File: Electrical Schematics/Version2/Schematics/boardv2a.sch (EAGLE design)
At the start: 622 parts, among them IC1 MCP41HVX1ST, IC2 ADUM4160BRW, IC3 SE555D, IC5 74LVC1G04DBV, IC6 74LVC1G04DBV, IC7 4030D, K1 G5V-2, K2 CP1SA-12V, Q1 IRLML2060TRPBFBSS123LT1G, Q10 IRLML2060TRPBFBSS123LT1G, Q11 IRLML2060TRPBFBSS123LT1G, Q12 IRLML2060TRPBFBSS123LT1G, Q13 IRLML2060TRPBFBSS123LT1G, Q17 IRLML2060TRPBFBSS123LT1G, Q18 MOSFET-PCHANNEL, Q19 IRLML2060TRPBFBSS123LT1G, Q2 IRLML2060TRPBFBSS123LT1G, Q3 IRLML2060TRPBFBSS123LT1G, Q4 MOSFET-PCHANNEL, Q5 MOSFET-PCHANNEL, Q6 IRLML2060TRPBFBSS123LT1G, Q7 ASFL1, Q8 IRLML2060TRPBFBSS123LT1G, Q9 IRLML2060TRPBFBSS123LT1G, U1 CP2130-GM, U10 SN65HVDA100-Q1_D_8, U11 ADUM3442CRWZ, U12 ADUM3442CRWZ, U13 ADUM3442CRWZ, U14 ADUM3442CRWZ, U15 ADUM3442CRWZ, U16 ADUM3442CRWZ, U17 ADUM3442CRWZ, U18 LM1085_KTT_3, U19 ADUM3442CRWZ, U2 TMS570LS0432_PZ_100, U20 ADUM3442CRWZ, U3 LM1085_KTT_3, U4 LM1085_KTT_3, U5 LM1084_KTT_3, U6 TPS3514_D_14, U7 LM1085_KTT_3, U9 ADUM3442CRWZ, X4 5566-4

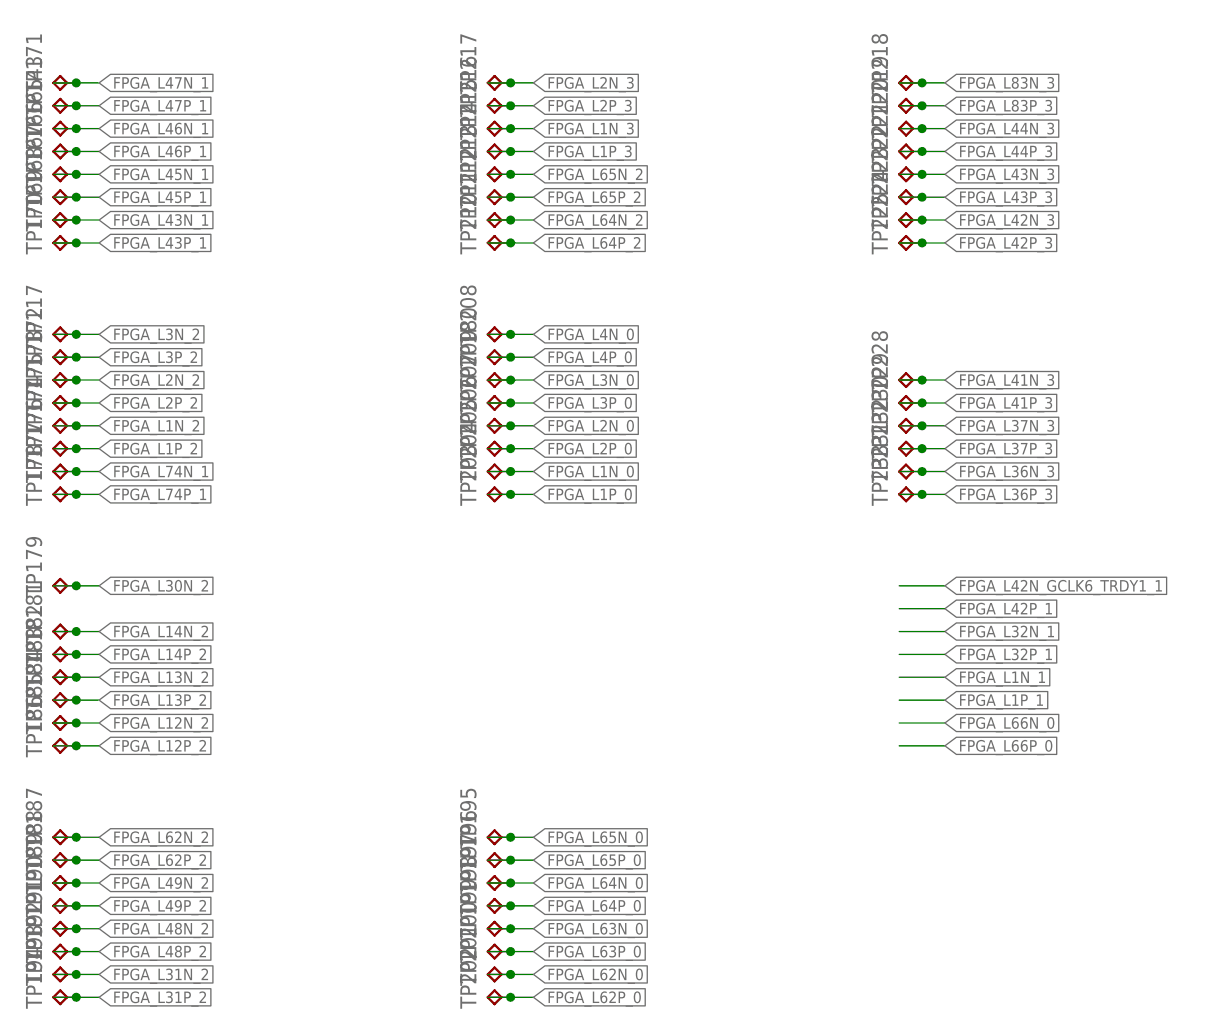
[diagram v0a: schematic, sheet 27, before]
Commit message: fpga to mcu
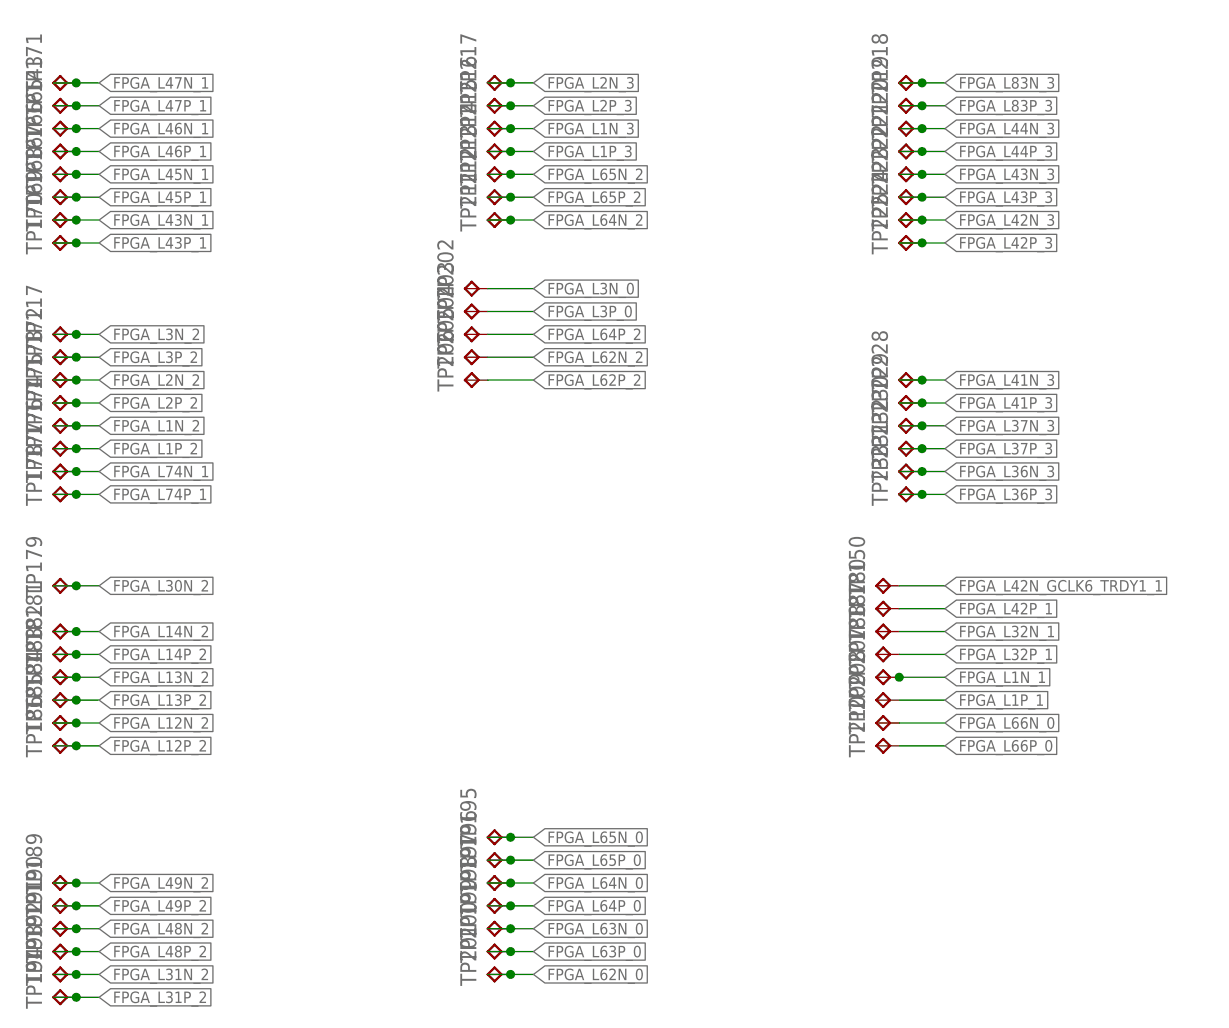
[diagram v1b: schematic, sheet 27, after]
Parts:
- added TP150: TPPAD1-13, testpad:TPPAD1-13
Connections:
- net FPGA_MCU_AD1_RES renamed N$307
- net FPGA_MCU_AD2_RES renamed N$308
- net FPGA_MCU_AD3_RES renamed N$309
- net FPGA_MCU_AD4_RES renamed N$310
- net FPGA_MCU_AD5_RES renamed N$311
- net FPGA_MCU_AD6_RES renamed N$312
- net FPGA_MCU_ADO_RES renamed N$306
- removed net FPGA_L1N_0: TP204.TP, U$6.IO_L1N_VREF_0
- removed net FPGA_L1P_0: TP203.TP, U$6.IO_L1P_HSWAPEN_0
- removed net FPGA_L2N_0: TP206.TP, U$6.IO_L2N_0
- removed net FPGA_L2P_0: TP205.TP, U$6.IO_L2P_0
- removed net FPGA_L4N_0: TP208.TP
- removed net FPGA_L4P_0: TP180.TP
- removed net FPGA_L62P_0: TP202.TP
- removed net FPGA_MCU_RES: U$6.IO_L3N_0
- new net N$313: TP140.TP, U2.ADIN[6]
- net FPGA_L1N_1: now also TP207.TP
- net FPGA_L1P_1: now also TP208.TP
- net FPGA_L32N_1: now also TP187.TP
- net FPGA_L32P_1: now also TP188.TP
- net FPGA_L3N_0: now also TP202.TP, U$6.IO_L3N_0; no longer TP209.TP
- net FPGA_L3P_0: now also TP203.TP, U$6.IO_L3P_0; no longer TP207.TP
- net FPGA_L42N_GCLK6_TRDY1_1: now also TP150.TP
- net FPGA_L42P_1: now also TP180.TP
- net FPGA_L62N_2: now also TP205.TP, U$6.IO_L62N_D6_2; no longer TP187.TP
- net FPGA_L62P_2: now also TP206.TP, U$6.IO_L62P_D5_2; no longer TP188.TP
- net FPGA_L64P_2: now also TP204.TP, U$6.IO_L64P_D8_2; no longer TP210.TP
- net FPGA_L66N_0: now also TP209.TP
- net FPGA_L66P_0: now also TP210.TP
- net FPGA_MCU_AD7_RES: no longer TP140.TP, U2.ADIN[6]
- net FPGA_MCU_RES1: now also U$6.IO_L1P_HSWAPEN_0; no longer U$6.IO_L3P_0
- net FPGA_MCU_RES2: now also U$6.IO_L1N_VREF_0; no longer U$6.IO_L64P_D8_2
- net FPGA_MCU_RES3: now also U$6.IO_L2P_0; no longer U$6.IO_L62N_D6_2
- net FPGA_MCU_RES4: now also U$6.IO_L2N_0; no longer U$6.IO_L62P_D5_2
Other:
- moved on the sheet: TP180, TP187, TP188, TP202, TP203, TP204, TP205, TP206, TP207, TP208, TP209, TP210

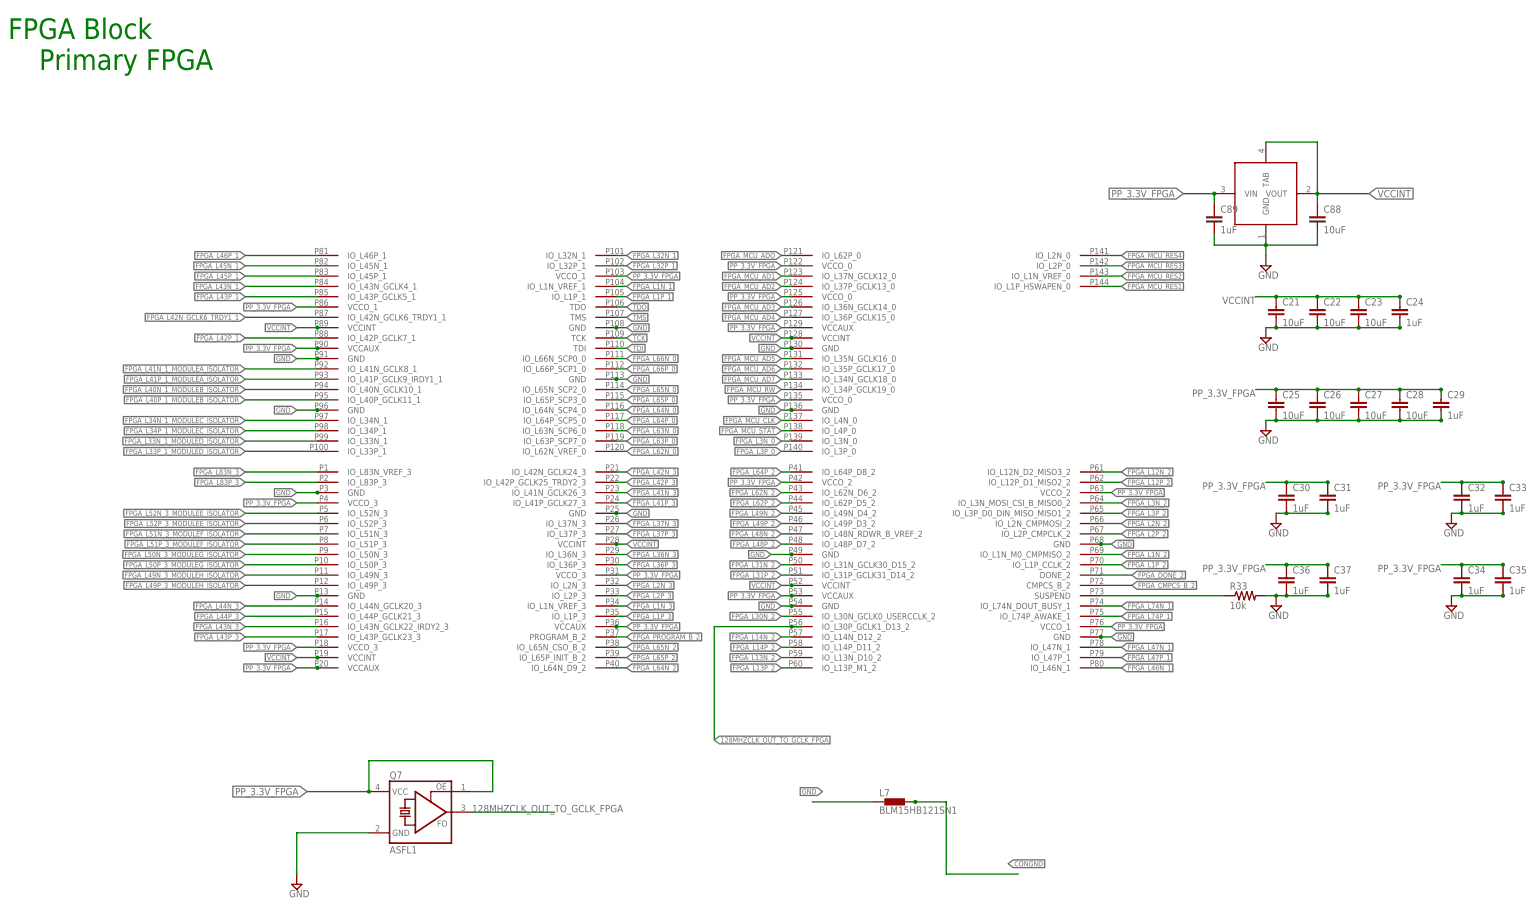
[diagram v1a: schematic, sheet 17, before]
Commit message: Fixed FPGA isolation routing
TODO: Check the FPGA pin by pin in the datasheet.
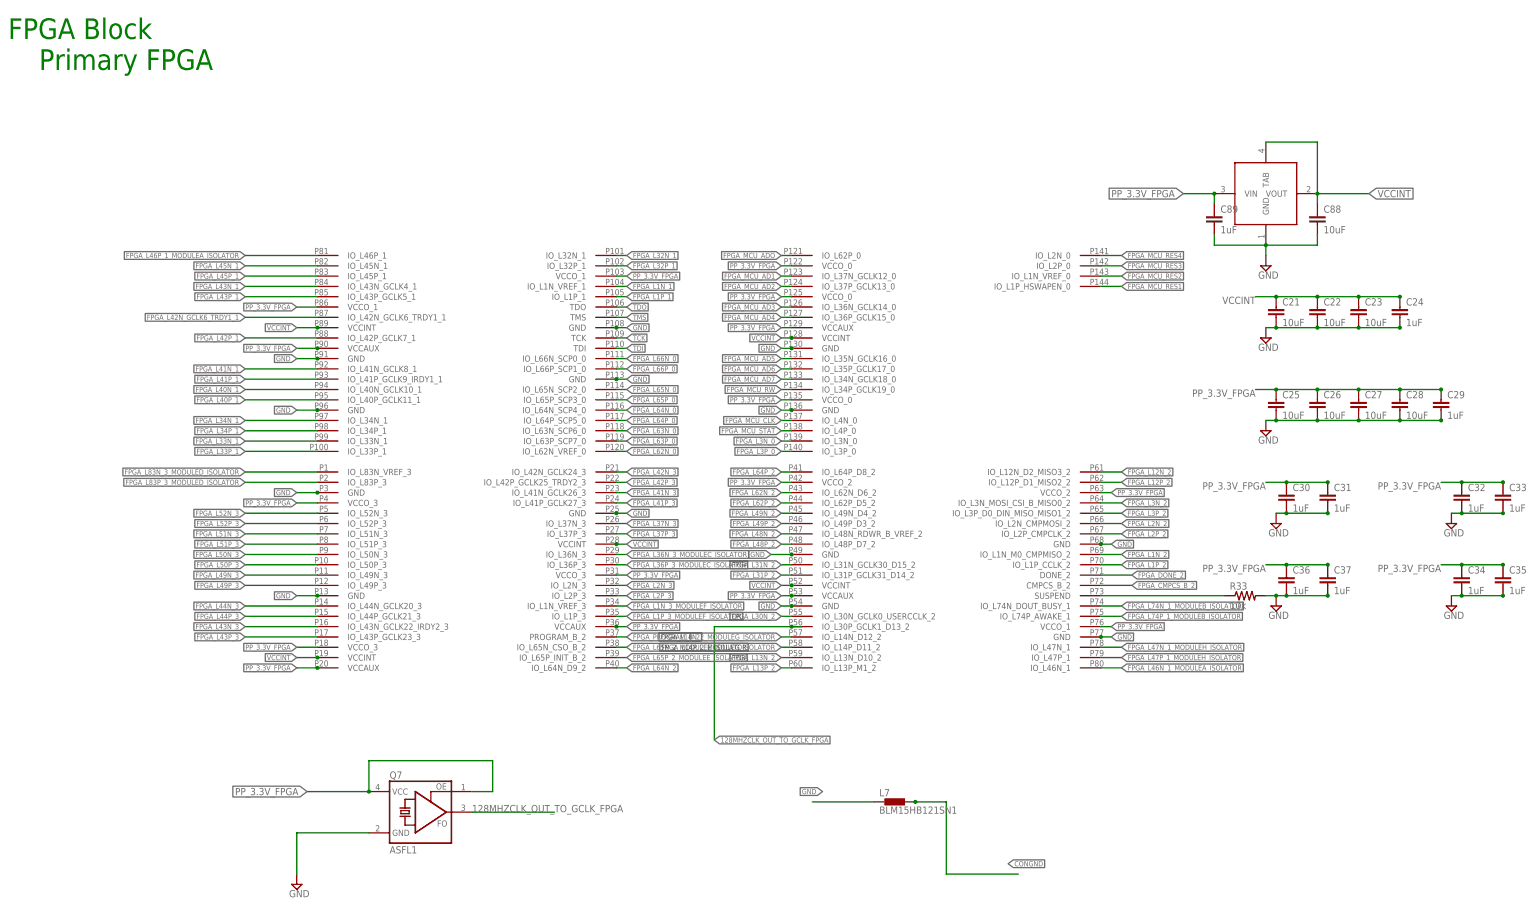
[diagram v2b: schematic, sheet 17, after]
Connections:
- removed net FPGA_L14N_2: TP181.TP, U$6.IO_L14N_D12_2
- removed net FPGA_L14P_2: TP182.TP, U$6.IO_L14P_D11_2
- removed net FPGA_L1N_3: TP215.TP, U$6.IO_L1N_VREF_3
- removed net FPGA_L1P_3: TP214.TP, U$6.IO_L1P_3
- removed net FPGA_L33N_1_MODULED_ISOLATOR: U$20.COM2, U$6.IO_L33N_1
- removed net FPGA_L33P_1_MODULED_ISOLATOR: U$23.COM2, U$6.IO_L33P_1
- removed net FPGA_L34N_1_MODULEC_ISOLATOR: U$18.COM2, U$6.IO_L34N_1
- removed net FPGA_L34P_1_MODULEC_ISOLATOR: U$19.COM2, U$6.IO_L34P_1
- removed net FPGA_L36N_3: TP231.TP, U$6.IO_L36N_3
- removed net FPGA_L36P_3: TP233.TP, U$6.IO_L36P_3
- removed net FPGA_L40N_1_MODULEB_ISOLATOR: U$16.COM2, U$6.IO_L40N_GCLK10_1
- removed net FPGA_L40P_1_MODULEB_ISOLATOR: U$17.COM2, U$6.IO_L40P_GCLK11_1
- removed net FPGA_L41N_1_MODULEA_ISOLATOR: U$13.COM2, U$6.IO_L41N_GCLK8_1
- removed net FPGA_L41P_1_MODULEA_ISOLATOR: U$14.COM2, U$6.IO_L41P_GCLK9_IRDY1_1
- removed net FPGA_L46N_1: TP165.TP, U$6.IO_L46N_1
- removed net FPGA_L46P_1: TP166.TP, U$6.IO_L46P_1
- removed net FPGA_L47N_1: TP171.TP, U$6.IO_L47N_1
- removed net FPGA_L47P_1: TP143.TP, U$6.IO_L47P_1
- removed net FPGA_L49N_3_MODULEH_ISOLATOR: U$30.COM2, U$6.IO_L49N_3
- removed net FPGA_L49P_3_MODULEH_ISOLATOR: U$31.COM2, U$6.IO_L49P_3
- removed net FPGA_L50N_3_MODULEG_ISOLATOR: U$28.COM2, U$6.IO_L50N_3
- removed net FPGA_L50P_3_MODULEG_ISOLATOR: U$29.COM2, U$6.IO_L50P_3
- removed net FPGA_L51N_3_MODULEF_ISOLATOR: U$26.COM2, U$6.IO_L51N_3
- removed net FPGA_L51P_3_MODULEF_ISOLATOR: U$27.COM2, U$6.IO_L51P_3
- removed net FPGA_L52N_3_MODULEE_ISOLATOR: U$24.COM2, U$6.IO_L52N_3
- removed net FPGA_L52P_3_MODULEE_ISOLATOR: U$25.COM2, U$6.IO_L52P_3
- removed net FPGA_L65N_2: TP213.TP, U$6.IO_L65N_CSO_B_2
- removed net FPGA_L65P_2: TP212.TP, U$6.IO_L65P_INIT_B_2
- removed net FPGA_L74N_1: TP177.TP, U$6.IO_L74N_DOUT_BUSY_1
- removed net FPGA_L74P_1: TP178.TP, U$6.IO_L74P_AWAKE_1
- removed net FPGA_L83N_3: TP218.TP, U$6.IO_L83N_VREF_3
- removed net FPGA_L83P_3: TP219.TP, U$6.IO_L83P_3
- new net FPGA_L14N_2_MODULEG_ISOLATOR: U$28.COM2, U$6.IO_L14N_D12_2
- new net FPGA_L14P_2_MODULEG_ISOLATOR: U$29.COM2, U$6.IO_L14P_D11_2
- new net FPGA_L1N_3_MODULEF_ISOLATOR: U$27.COM2, U$6.IO_L1N_VREF_3
- new net FPGA_L1P_3_MODULEF_ISOLATOR: U$26.COM2, U$6.IO_L1P_3
- new net FPGA_L33N_1: TP218.TP, U$6.IO_L33N_1
- new net FPGA_L33P_1: TP219.TP, U$6.IO_L33P_1
- new net FPGA_L34N_1: TP231.TP, U$6.IO_L34N_1
- new net FPGA_L34P_1: TP233.TP, U$6.IO_L34P_1
- new net FPGA_L36N_3_MODULEC_ISOLATOR: U$19.COM2, U$6.IO_L36N_3
- new net FPGA_L36P_3_MODULEC_ISOLATOR: U$18.COM2, U$6.IO_L36P_3
- new net FPGA_L40N_1: TP177.TP, U$6.IO_L40N_GCLK10_1
- new net FPGA_L40P_1: TP178.TP, U$6.IO_L40P_GCLK11_1
- new net FPGA_L41N_1: TP165.TP, U$6.IO_L41N_GCLK8_1
- new net FPGA_L41P_1: TP166.TP, U$6.IO_L41P_GCLK9_IRDY1_1
- new net FPGA_L46N_1_MODULEA_ISOLATOR: U$13.COM2, U$6.IO_L46N_1
- new net FPGA_L46P_1_MODULEA_ISOLATOR: U$14.COM2, U$6.IO_L46P_1
- new net FPGA_L47N_1_MODULEH_ISOLATOR: U$30.COM2, U$6.IO_L47N_1
- new net FPGA_L47P_1_MODULEH_ISOLATOR: U$31.COM2, U$6.IO_L47P_1
- new net FPGA_L49N_3: TP171.TP, U$6.IO_L49N_3
- new net FPGA_L49P_3: TP143.TP, U$6.IO_L49P_3
- new net FPGA_L50N_3: TP181.TP, U$6.IO_L50N_3
- new net FPGA_L50P_3: TP182.TP, U$6.IO_L50P_3
- new net FPGA_L51N_3: TP215.TP, U$6.IO_L51N_3
- new net FPGA_L51P_3: TP214.TP, U$6.IO_L51P_3
- new net FPGA_L52N_3: TP213.TP, U$6.IO_L52N_3
- new net FPGA_L52P_3: TP212.TP, U$6.IO_L52P_3
- new net FPGA_L65N_2_MODULEE_ISOLATOR: U$24.COM2, U$6.IO_L65N_CSO_B_2
- new net FPGA_L65P_2_MODULEE_ISOLATOR: U$25.COM2, U$6.IO_L65P_INIT_B_2
- new net FPGA_L74N_1_MODULEB_ISOLATOR: U$16.COM2, U$6.IO_L74N_DOUT_BUSY_1
- new net FPGA_L74P_1_MODULEB_ISOLATOR: U$17.COM2, U$6.IO_L74P_AWAKE_1
- new net FPGA_L83N_3_MODULED_ISOLATOR: U$23.COM2, U$6.IO_L83N_VREF_3
- new net FPGA_L83P_3_MODULED_ISOLATOR: U$20.COM2, U$6.IO_L83P_3

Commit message: routed more traces
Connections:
- net 5V_SU_J renamed 5V_SU_J123
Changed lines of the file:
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@@
 </segment>
 </net>
-<net name="5V_SU_J" class="0">
+<net name="5V_SU_J123" class="0">
 <segment>
 <wire x1="26.67" y1="90.17" x2="27.94" y2="90.17" width="0.1524" layer="91"/>

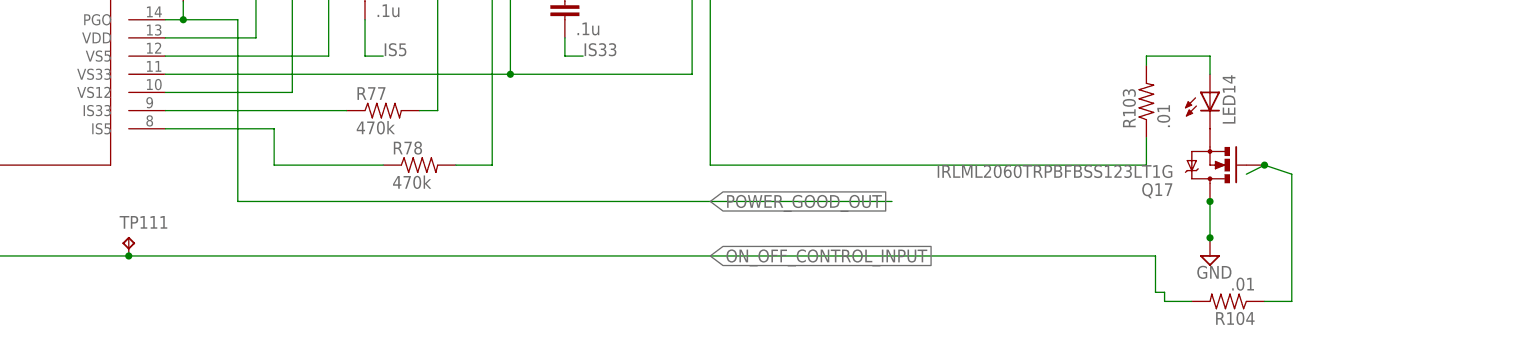
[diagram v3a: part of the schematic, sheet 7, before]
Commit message: Cap Placement and routing
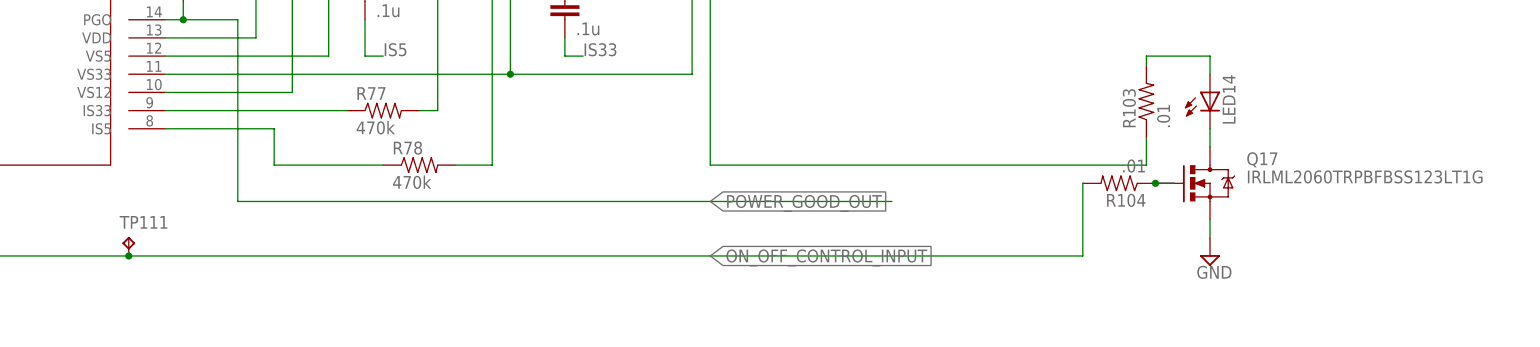
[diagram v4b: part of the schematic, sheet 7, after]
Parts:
- added C17: 10uF, SparkFun-Capacitors:CAP0603-CAP
- added C18: 1uF, SparkFun-Capacitors:CAP0603-CAP
- added R34, R41, R42: 10k, SparkFun-Passives:RESISTOR0603-RES
- added U$33: 1.2VREG, shit:1.2VREG
- TP216, TP217: value TPPAD1-13 -> TPB1,27; device testpad:TPPAD1-13 -> testpad:TPB1,27
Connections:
- removed net FPGA_L2N_3: TP217.TP, U$6.IO_L2N_3
- removed net FPGA_L2P_3: TP216.TP, U$6.IO_L2P_3
- removed net FPGA_L65N_2_MODULEE_ISOLATOR: U$24.COM2, U$6.IO_L65N_CSO_B_2
- removed net FPGA_L65P_2_MODULEE_ISOLATOR: U$25.COM2, U$6.IO_L65P_INIT_B_2
- removed net N$115: LED14.C, Q17.S
- new net FPGA_L2N_3_MODULEE_ISOLATOR: U$24.COM2, U$6.IO_L1N_VREF_3
- new net FPGA_L2P_3_MODULEE_ISOLATOR: U$25.COM2, U$6.IO_L1P_3
- new net FPGA_L65N_2: U$6.IO_L65N_CSO_B_2
- new net FPGA_PROGRAM_B: R42.1, U$6.IO_L65P_INIT_B_2
- new net N$12: LED14.C, Q17.D
- net CON_MONB_-: now also U19.GND2, U20.GND2
- net FPGA_DONE_2: now also R34.1
- net FPGA_L1N_3_MODULEF_ISOLATOR: now also U$6.IO_L2N_3; no longer U$6.IO_L1N_VREF_3
- net FPGA_L1P_3_MODULEF_ISOLATOR: now also U$6.IO_L2P_3; no longer U$6.IO_L1P_3
- net FPGA_PROGRAM_B_2: now also R41.1
- net GND: now also C17.2, C18.2, Q12.S, Q17.S, U$33.GND; no longer Q12.D, Q17.D
- net MCU_+1.2V: now also C17.1, U$33.TAB, U$33.VOUT
- net MCU_+3.3V: now also C18.1, U$33.VIN
- net N$185: now also TP216.TP
- net N$193: now also TP217.TP
- net N$26: now also R2401.2
- net N$63: now also Q12.D; no longer Q12.S
- net PP_3.3V_FPGA: now also R34.2, R41.2, R42.2
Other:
- moved on the sheet: Q12, Q17, R104, R2401, R29

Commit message: connector and routing
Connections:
- removed net CON_RELAY_HIGHSIDE: X4-4.S
- removed net FNR_CON_GROUND: U$5.P$6
- net 12V_SUPERVISED: now also U$5.P$6; no longer U$5.P$19
- net 5V_SUPERVISED: now also X4-4.S
- net CON_FIN: now also U$5.P$16; no longer U$5.P$14
- net CON_FNR_HIGH: now also U$5.P$11; no longer U$5.P$18
- net CON_FNR_POTGND: now also U$5.P$12; no longer U$5.P$16
- net CON_MONB_+: now also U$5.P$4; no longer U$5.P$9
- net CON_MONB_-: now also U$5.P$5; no longer U$5.P$10
- net CON_MONC_+: now also U$5.P$9; no longer U$5.P$11
- net CON_MONC_-: now also U$5.P$20; no longer U$5.P$12
- net CON_MONC_SP: now also U$5.P$10; no longer U$5.P$17
- net CON_NIN: now also U$5.P$17; no longer U$5.P$15
- net FNR_CON_F: now also U$5.P$15; no longer U$5.P$1
- net FNR_CON_R: now also U$5.P$14; no longer U$5.P$2
- net FNR_CON_THROTTLE-: now also U$5.P$2; no longer U$5.P$4
- net FNR_CON_THROTTLEWIPER: now also U$5.P$1; no longer U$5.P$5
- net GND: now also U$5.P$18, U$5.P$19; no longer U$5.P$20
